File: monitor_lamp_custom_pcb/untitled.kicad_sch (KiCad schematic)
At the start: 14 parts, among them J10 Conn_01x01, J2 VEML7700_Connection, J3 LD2410C_Connection, J4 Conn_01x02, J5 SHTxx_Connection, J7 Conn_01x01, J8 Conn_01x01, J9 Conn_01x01, Q3 AO3400A, U3 ESP32-C3_SUPERMINI_TH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

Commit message: Changed all resistors footprint to R_0603_1608 metric
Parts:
- R5: footprint Resistor_SMD:R_0402_1005Metric -> Resistor_SMD:R_0603_1608Metric
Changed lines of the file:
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@@
 			)
 		)
-		(property "Footprint" "Resistor_SMD:R_0402_1005Metric"
+		(property "Footprint" "Resistor_SMD:R_0603_1608Metric"
 			(at 141.732 110.49 90)
 			(hide yes)

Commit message: Added some LCSC to the components
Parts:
- removed D1: 1N5819WS, Diode_SMD:D_SOD-323, symbol Diode:1N5819WS
- added D1: SS34, Diode_SMD:D_SMA, symbol Diode:SS34
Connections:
- net +12V_Input: now also D1.1 (K)
- net at J4.2 (Pin_2), Q3.2 (S): now also D1.2 (A)
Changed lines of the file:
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@@
 	(paper "A4")
+	(junction
+		(at 191.77 132.08)
+		(diameter 0)
+		(color 0 0 0 0)
+	)
 	(junction
 		(at 224.79 53.34)
@@
 	)
 	(junction
-		(at 185.42 132.08)
+		(at 191.77 124.46)
 		(diameter 0)
 		(color 0 0 0 0)
@@
 	)
 	(junction
-		(at 185.42 124.46)
-		(diameter 0)
-		(color 0 0 0 0)
-	)
-	(junction
 		(at 143.51 116.84)
 		(diameter 0)
@@
 	(wire
 		(pts
-			(xy 176.53 124.46) (xy 185.42 124.46)
-		)
-		(stroke
-			(width 0)
-			(type default)
-		)
-	)
-	(wire
-		(pts
-			(xy 185.42 132.08) (xy 204.47 132.08)
+			(xy 176.53 124.46) (xy 191.77 124.46)
 		)
 		(stroke
@@
 	(wire
 		(pts
+			(xy 191.77 124.46) (xy 200.66 124.46)
+		)
+		(stroke
+			(width 0)
+			(type default)
+		)
+	)
+	(wire
+		(pts
 			(xy 96.52 54.61) (xy 96.52 63.5)
 		)
@@
 	(wire
 		(pts
-			(xy 148.59 132.08) (xy 185.42 132.08)
+			(xy 148.59 132.08) (xy 191.77 132.08)
+		)
+		(stroke
+			(width 0)
+			(type default)
+		)
+	)
+	(wire
+		(pts
+			(xy 191.77 132.08) (xy 204.47 132.08)
 		)
 		(stroke
@@
 		(pts
 			(xy 200.66 129.54) (xy 200.66 124.46)
-		)
-		(stroke
-			(width 0)
-			(type default)
-		)
-	)
-	(wire
-		(pts
-			(xy 200.66 124.46) (xy 185.42 124.46)
 		)
 		(stroke
@@
 	)
 	(symbol
+		(lib_id "Diode:SS34")
+		(at 191.77 128.27 270)
+		(unit 1)
+		(body_style 1)
+		(exclude_from_sim no)
+		(in_bom yes)
+		(on_board yes)
+		(in_pos_files yes)
+		(dnp no)
+		(fields_autoplaced yes)
+		(property "Reference" "D1"
+			(at 194.31 126.6824 90)
+			(show_name no)
+			(do_not_autoplace no)
+			(effects
+				(font
+					(size 1.27 1.27)
+				)
+				(justify left)
+			)
+		)
+		(property "Value" "SS34"
+			(at 194.31 129.2224 90)
+			(show_name no)
+			(do_not_autoplace no)
+			(effects
+				(font
+					(size 1.27 1.27)
+				)
+				(justify left)
+			)
+		)
+		(property "Footprint" "Diode_SMD:D_SMA"
+			(at 187.325 128.27 0)
+			(hide yes)
+			(show_name no)
+			(do_not_autoplace no)
+			(effects
+				(font
+					(size 1.27 1.27)
+				)
+			)
+		)
+		(property "Datasheet" "https://www.vishay.com/docs/88751/ss32.pdf"
+			(at 191.77 128.27 0)
+			(hide yes)
+			(show_name no)
+			(do_not_autoplace no)
+			(effects
+				(font
+					(size 1.27 1.27)
+				)
+			)
+		)
+		(property "Description" "40V 3A Schottky Diode, SMA"
+			(at 191.77 128.27 0)
+			(hide yes)
+			(show_name no)
+			(do_not_autoplace no)
+			(effects
+				(font
+					(size 1.27 1.27)
+				)
+			)
+		)
+		(property "LCSC" "C8678"
+			(at 191.77 128.27 90)
+			(hide yes)
+			(show_name no)
+			(do_not_autoplace no)
+			(effects
+				(font
+					(size 1.27 1.27)
+				)
+			)
+		)
+		(pin "1"
+		)
+		(pin "2"
+		)
+		(instances
+			(project "monitor_lamp_custom_pcb"
+				(path "/77ed2f8f-6c9e-49d8-b473-d071fcc9ba2f/0d662d48-a846-4d52-8851-1394daa2469c"
+					(reference "D1")
+					(unit 1)
+				)
+			)
+		)
+	)
+	(symbol
 		(lib_id "power:GND")
 		(at 48.26 177.8 0)
@@
 					(unit 1)
 				)
-			)
-		)
-	)
-	(symbol
-		(lib_id "Diode:1N5819WS")
-		(at 185.42 128.27 270)
-		(unit 1)
-		(body_style 1)
-		(exclude_from_sim no)
-		(in_bom yes)
-		(on_board yes)
-		(in_pos_files yes)
-		(dnp no)
-		(fields_autoplaced yes)
-		(property "Reference" "D1"
-			(at 187.96 126.6824 90)
-			(show_name no)
-			(do_not_autoplace no)
-			(effects
-				(font
-					(size 1.27 1.27)
-				)
-				(justify left)
-			)
-		)
-		(property "Value" "1N5819WS"
-			(at 187.96 129.2224 90)
-			(show_name no)
-			(do_not_autoplace no)
-			(effects
-				(font
-					(size 1.27 1.27)
-				)
-				(justify left)
-			)
-		)
-		(property "Footprint" "Diode_SMD:D_SOD-323"
-			(at 180.975 128.27 0)
-			(hide yes)
-			(show_name no)
-			(do_not_autoplace no)
-			(effects
-				(font
-					(size 1.27 1.27)
-				)
-			)
-		)
-		(property "Datasheet" "https://datasheet.lcsc.com/lcsc/2204281430_Guangdong-Hottech-1N5819WS_C191023.pdf"
-			(at 185.42 128.27 0)
-			(hide yes)
-			(show_name no)
-			(do_not_autoplace no)
-			(effects
-				(font
-					(size 1.27 1.27)
-				)
-			)
-		)
-		(property "Description" "40V 600mV@1A 1A SOD-323 Schottky Barrier Diodes, SOD-323"
-			(at 185.42 128.27 0)
-			(hide yes)
-			(show_name no)
-			(do_not_autoplace no)
-			(effects
-				(font
-					(size 1.27 1.27)
-				)
-			)
-		)
-		(pin "1"
-		)
-		(pin "2"
-		)
-		(instances
-			(project "monitor_lamp_custom_pcb"
-				(path "/77ed2f8f-6c9e-49d8-b473-d071fcc9ba2f/0d662d48-a846-4d52-8851-1394daa2469c"
-					(reference "D1")
-					(unit 1)
-				)

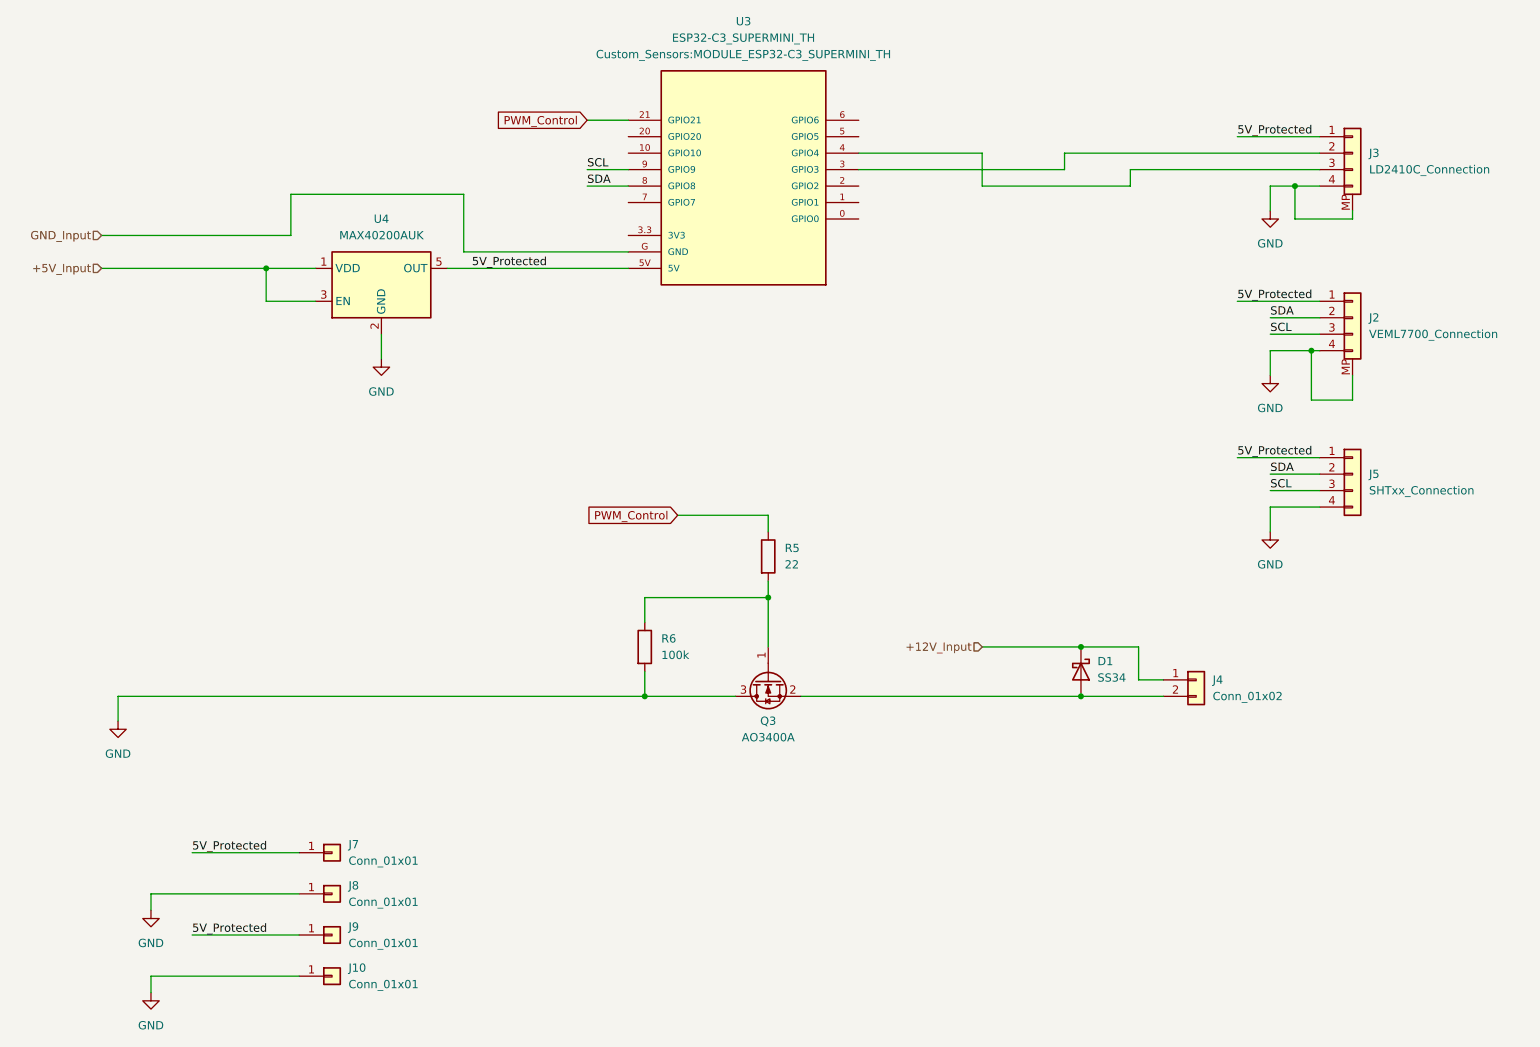
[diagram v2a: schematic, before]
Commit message: Assign LCSC number to some component and selected new voltage regulator
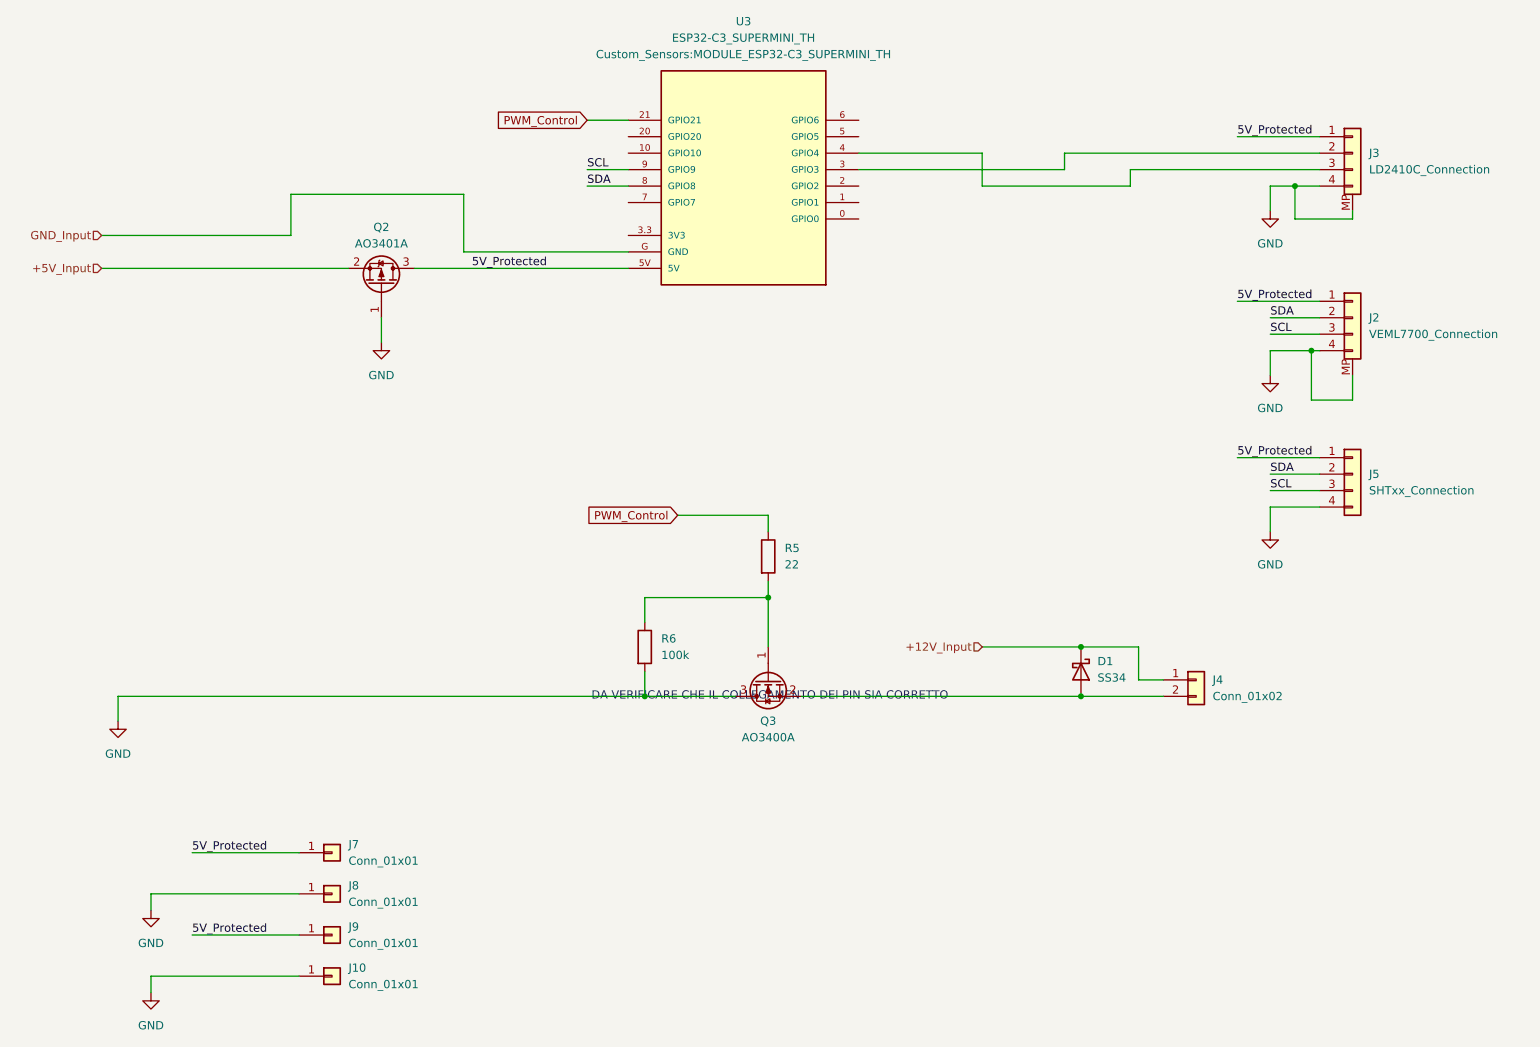
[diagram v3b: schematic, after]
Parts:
- removed U4: MAX40200AUK, Package_TO_SOT_SMD:SOT-23-5, symbol Analog_Switch:MAX40200AUK
- added Q2: AO3401A, Package_TO_SOT_SMD:SOT-23, symbol Transistor_FET:AO3401A
- Q3: LCSC (none) -> C20917
- R5: LCSC (none) -> C23345
- R6: LCSC (none) -> C25803
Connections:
- net +5V_Input: now also Q2.2 (S)
- net 5V_Protected: now also Q2.3 (D)
- net GND: now also Q2.1 (G)
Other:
- note added: "DA VERIFICARE CHE IL COLLEGAMENTO DEI PIN SIA CORRETTO"
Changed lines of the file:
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@@
 	(generator_version "10.0")
 	(paper "A4")
+	(text "DA VERIFICARE CHE IL COLLEGAMENTO DEI PIN SIA CORRETTO\n"
+		(exclude_from_sim no)
+		(at 143.764 132.08 0)
+		(effects
+			(font
+				(size 1.27 1.27)
+			)
+		)
+	)
 	(junction
 		(at 191.77 132.08)
@@
 	)
 	(junction
-		(at 66.04 66.04)
-		(diameter 0)
-		(color 0 0 0 0)
-	)
-	(junction
 		(at 143.51 116.84)
 		(diameter 0)
@@
 	(wire
 		(pts
-			(xy 93.98 66.04) (xy 121.92 66.04)
-		)
-		(stroke
-			(width 0)
-			(type default)
-		)
-	)
-	(wire
-		(pts
 			(xy 220.98 100.33) (xy 228.6 100.33)
 		)
@@
 	(wire
 		(pts
-			(xy 66.04 66.04) (xy 66.04 71.12)
-		)
-		(stroke
-			(width 0)
-			(type default)
-		)
-	)
-	(wire
-		(pts
 			(xy 176.53 48.26) (xy 157.48 48.26)
 		)
@@
 	(wire
 		(pts
-			(xy 83.82 76.2) (xy 83.82 80.01)
+			(xy 83.82 73.66) (xy 83.82 77.47)
 		)
 		(stroke
@@
 	(wire
 		(pts
+			(xy 88.9 66.04) (xy 121.92 66.04)
+		)
+		(stroke
+			(width 0)
+			(type default)
+		)
+	)
+	(wire
+		(pts
 			(xy 48.26 162.56) (xy 48.26 165.1)
 		)
@@
 	(wire
 		(pts
-			(xy 73.66 71.12) (xy 66.04 71.12)
-		)
-		(stroke
-			(width 0)
-			(type default)
-		)
-	)
-	(wire
-		(pts
 			(xy 200.66 129.54) (xy 200.66 124.46)
 		)
@@
 	(wire
 		(pts
-			(xy 40.64 66.04) (xy 66.04 66.04)
-		)
-		(stroke
-			(width 0)
-			(type default)
-		)
-	)
-	(wire
-		(pts
-			(xy 66.04 66.04) (xy 73.66 66.04)
+			(xy 40.64 66.04) (xy 78.74 66.04)
 		)
 		(stroke
@@
 	(symbol
 		(lib_id "power:GND")
-		(at 83.82 80.01 0)
+		(at 83.82 77.47 0)
 		(unit 1)
 		(body_style 1)
@@
 		(fields_autoplaced yes)
 		(property "Reference" "#PWR010"
-			(at 83.82 86.36 0)
+			(at 83.82 83.82 0)
 			(hide yes)
 			(show_name no)
@@
 		)
 		(property "Value" "GND"
-			(at 83.82 85.09 0)
+			(at 83.82 82.55 0)
 			(show_name no)
 			(do_not_autoplace no)
@@
 		)
 		(property "Footprint" ""
-			(at 83.82 80.01 0)
+			(at 83.82 77.47 0)
 			(hide yes)
 			(show_name no)
@@
 		)
 		(property "Datasheet" ""
-			(at 83.82 80.01 0)
+			(at 83.82 77.47 0)
 			(hide yes)
 			(show_name no)
@@
 		)
 		(property "Description" "Power symbol creates a global label with name \"GND\" , ground"
-			(at 83.82 80.01 0)
+			(at 83.82 77.47 0)
 			(hide yes)
 			(show_name no)
@@
 				(path "/77ed2f8f-6c9e-49d8-b473-d071fcc9ba2f/0d662d48-a846-4d52-8851-1394daa2469c"
 					(reference "#PWR010")
-					(unit 1)
-				)
-			)
-		)
-	)
-	(symbol
-		(lib_id "Analog_Switch:MAX40200AUK")
-		(at 83.82 68.58 0)
-		(unit 1)
-		(body_style 1)
-		(exclude_from_sim no)
-		(in_bom yes)
-		(on_board yes)
-		(in_pos_files yes)
-		(dnp no)
-		(fields_autoplaced yes)
-		(property "Reference" "U4"
-			(at 83.82 58.42 0)
-			(show_name no)
-			(do_not_autoplace no)
-			(effects
-				(font
-					(size 1.27 1.27)
-				)
-			)
-		)
-		(property "Value" "MAX40200AUK"
-			(at 83.82 60.96 0)
-			(show_name no)
-			(do_not_autoplace no)
-			(effects
-				(font
-					(size 1.27 1.27)
-				)
-			)
-		)
-		(property "Footprint" "Package_TO_SOT_SMD:SOT-23-5"
-			(at 83.82 55.88 0)
-			(hide yes)
-			(show_name no)
-			(do_not_autoplace no)
-			(effects
-				(font
-					(size 1.27 1.27)
-				)
-			)
-		)
-		(property "Datasheet" "https://datasheets.maximintegrated.com/en/ds/MAX40200.pdf"
-			(at 83.82 55.88 0)
-			(hide yes)
-			(show_name no)
-			(do_not_autoplace no)
-			(effects
-				(font
-					(size 1.27 1.27)
-				)
-			)
-		)
-		(property "Description" "Ideal Diode, Ultra-Low Voltage Drop, 1.5-5.5V, 1A, SOT-23-5"
-			(at 83.82 68.58 0)
-			(hide yes)
-			(show_name no)
-			(do_not_autoplace no)
-			(effects
-				(font
-					(size 1.27 1.27)
-				)
-			)
-		)
-		(pin "4"
-		)
-		(pin "3"
-		)
-		(pin "1"
-		)
-		(pin "2"
-		)
-		(pin "5"
-		)
-		(instances
-			(project "monitor_lamp_custom_pcb"
-				(path "/77ed2f8f-6c9e-49d8-b473-d071fcc9ba2f/0d662d48-a846-4d52-8851-1394daa2469c"
-					(reference "U4")
 					(unit 1)
 				)
@@
 			)
 		)
+		(property "LCSC" "C25803"
+			(at 124.46 124.46 0)
+			(hide yes)
+			(show_name no)
+			(do_not_autoplace no)
+			(effects
+				(font
+					(size 1.27 1.27)
+				)
+			)
+		)
 		(pin "1"
 		)
@@
 				(path "/77ed2f8f-6c9e-49d8-b473-d071fcc9ba2f/0d662d48-a846-4d52-8851-1394daa2469c"
 					(reference "R6")
+					(unit 1)
+				)
+			)
+		)
+	)
+	(symbol
+		(lib_id "Transistor_FET:AO3401A")
+		(at 83.82 68.58 270)
+		(mirror x)
+		(unit 1)
+		(body_style 1)
+		(exclude_from_sim no)
+		(in_bom yes)
+		(on_board yes)
+		(in_pos_files yes)
+		(dnp no)
+		(property "Reference" "Q2"
+			(at 83.82 59.69 90)
+			(show_name no)
+			(do_not_autoplace no)
+			(effects
+				(font
+					(size 1.27 1.27)
+				)
+			)
+		)
+		(property "Value" "AO3401A"
+			(at 83.82 62.23 90)
+			(show_name no)
+			(do_not_autoplace no)
+			(effects
+				(font
+					(size 1.27 1.27)
+				)
+			)
+		)
+		(property "Footprint" "Package_TO_SOT_SMD:SOT-23"
+			(at 81.915 63.5 0)
+			(hide yes)
+			(show_name no)
+			(do_not_autoplace no)
+			(effects
+				(font
+					(size 1.27 1.27)
+					(italic yes)
+				)
+				(justify left)
+			)
+		)
+		(property "Datasheet" "http://www.aosmd.com/pdfs/datasheet/AO3401A.pdf"
+			(at 80.01 63.5 0)
+			(hide yes)
+			(show_name no)
+			(do_not_autoplace no)
+			(effects
+				(font
+					(size 1.27 1.27)
+				)
+				(justify left)
+			)
+		)
+		(property "Description" "-4.0A Id, -30V Vds, P-Channel MOSFET, SOT-23"
+			(at 83.82 68.58 0)
+			(hide yes)
+			(show_name no)
+			(do_not_autoplace no)
+			(effects
+				(font
+					(size 1.27 1.27)
+				)
+			)
+		)
+		(pin "2"
+		)
+		(pin "3"
+		)
+		(pin "1"
+		)
+		(instances
+			(project "monitor_lamp_custom_pcb"
+				(path "/77ed2f8f-6c9e-49d8-b473-d071fcc9ba2f/0d662d48-a846-4d52-8851-1394daa2469c"
+					(reference "Q2")
 					(unit 1)
 				)
@@
 			)
 		)
+		(property "LCSC" "C23345"
+			(at 143.51 110.49 0)
+			(hide yes)
+			(show_name no)
+			(do_not_autoplace no)
+			(effects
+				(font
+					(size 1.27 1.27)
+				)
+			)
+		)
 		(pin "1"
 		)
@@
 			(hide yes)
 			(show_name no)
+			(do_not_autoplace no)
+			(effects
+				(font
+					(size 1.27 1.27)
+				)
+			)
+		)
+		(property "LCSC" "C20917"
+			(at 143.51 129.54 90)
+			(hide yes)
+			(show_name no)

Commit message: Drastic change
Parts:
- Q2: LCSC (none) -> C15127
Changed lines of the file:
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@@
+			)
+		)
+		(property "LCSC" "C15127"
+			(at 83.82 68.58 90)
+			(hide yes)
+			(show_name no)
+			(do_not_autoplace no)
+			(effects
+				(font
+					(size 1.27 1.27)
+				)
 			)
 		)
